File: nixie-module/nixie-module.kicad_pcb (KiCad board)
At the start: 2 copper layers, 36 x 56 mm, 7 parts, among them P1 CONN_02X05, U1 74141

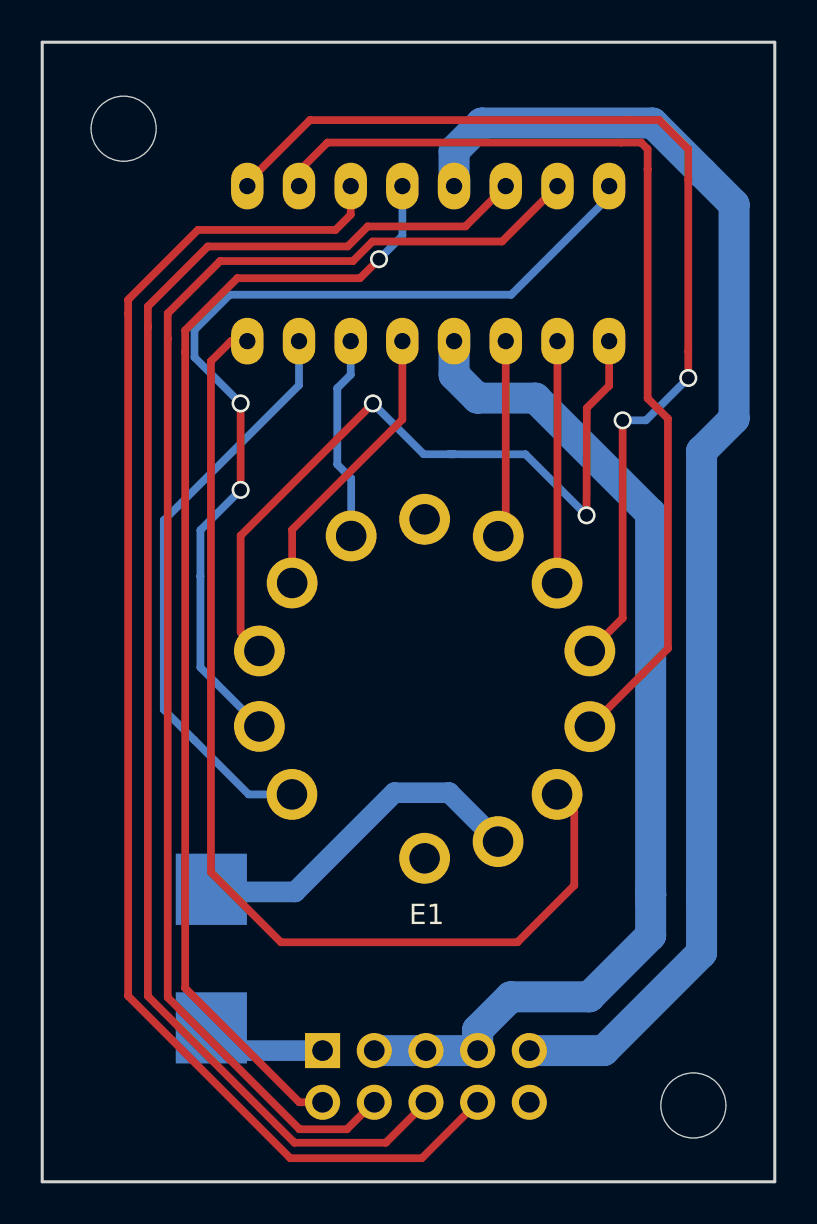
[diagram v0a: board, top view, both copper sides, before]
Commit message: poprawki prowadzenia ścieżek, footprintów, zmniejszenie rozmiaru płytki pod lampę nixie
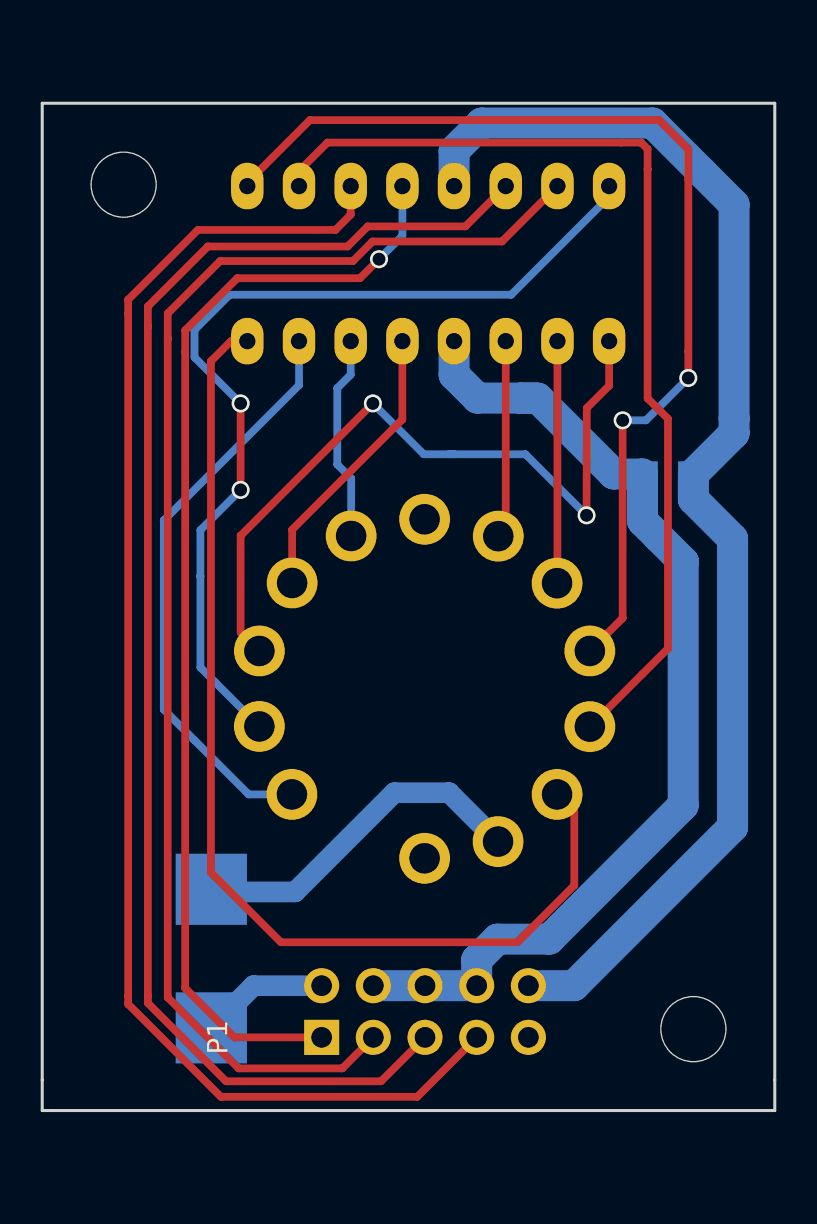
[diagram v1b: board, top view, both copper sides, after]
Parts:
- P1: footprint nixie-module-footprint:Pin_Header_Angled_2x05 -> Pin_Headers:Pin_Header_Straight_2x05; moved to F.Cu
- moved C1 20.7 mm to (158.8, 93.2)
- moved REF** 3.75 mm to (160.0, 120.5)
- moved REF** 2.75 mm to (132.0, 79.0)
- moved P1 0.65 mm to (141.7, 120.9), turned to 90 degrees
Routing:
- net VCC: track 65.6 -> 63.2 mm
- net Net-(P1-Pad2): track 5.93 -> 7.86 mm
- net /D: track 56.4 -> 55.1 mm
- net /C: track 68.7 -> 67.5 mm
- net /B: track 71.4 -> 70.4 mm
- net /A: track 69.9 -> 68.9 mm
- net GND: track 51.4 -> 50.4 mm
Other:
- board size 36 x 56 mm -> 36 x 49.5 mm
